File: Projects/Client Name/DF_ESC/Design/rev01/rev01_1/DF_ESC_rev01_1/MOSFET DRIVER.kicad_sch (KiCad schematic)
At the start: 40 parts, among them U1 DRV8302DCAR

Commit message: Update 2024-02-28_2
Input Proteccion Done
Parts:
- renumbered C2 to C?, C4 to C?, C3 to C?, D1 to D?, U1 to U?

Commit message: Update 2024-02-03
Schematic finish but DRC CHEK Errors
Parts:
- removed U?: DRV8302DCAR, DCA56_6P35X3P61, symbol DRV8302:DRV8302DCAR
- added U3: DRV8302DCAR, footprint:HTSSOP-56_L14.0-W6.1-P0.50-LS8.1-BL-EP, symbol Motor_Driver:DRV8302DCAR
- C26, C27, C28, C29, C30, C31, C32, C33, C34, C35, C36, C37, C38, C39, C40, C41, C42, C43, C44, C45, C46, C47, C48, C49: renamed from C?; footprint (none) -> Capacitor_SMD:C_0603_1608Metric_Pad1.08x0.95mm_HandSolder
- L1: renamed from L?; footprint (none) -> DF_ESC_Footprint_Library_Casa:IND-SMD_L7.8-W7.8_SDR0805
- R17, R18, R19, R20, R21, R22, R23, R24, R25, R26, R27, R28: renamed from R?; footprint (none) -> Resistor_SMD:R_0603_1608Metric_Pad0.98x0.95mm_HandSolder
- gave numbers to parts that had none: 2
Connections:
- net +3V3: now also U3.24 (REF), U3.9 (M_OC)
- net +VDC: now also U3.29 (PVDD1), U3.53 (PVDD2), U3.54 (PVDD2)
- net BIAS: now also U3.49 (BIAS)
- net BR_S01: now also U3.25 (SO1)
- net BR_S02: now also U3.26 (SO2)
- net BST_A: now also U3.48 (BST_A)
- net BST_B: now also U3.43 (BST_B)
- net BST_BK: now also U3.52 (BST_BK)
- net BST_C: now also U3.38 (BST_C)
- net COMP: now also U3.2 (COMP)
- net CP1: now also U3.14 (CP1)
- net CP2: now also U3.15 (CP2)
- net DC_CAL: now also U3.12 (DC_CAL)
- net DTC: now also U3.7 (DTC)
- net DVDD: now also U3.11 (OC_ADJ), U3.23 (DVDD)
- net EN_GATE: now also U3.16 (EN_GATE)
- net FAULT: now also U3.6 (nFAULT)
- net GND: now also U3.10 (GAIN), U3.28 (AGND), U3.57 (GND), U3.8 (M_PWM)
- net GVDD: now also U3.13 (GVDD)
- net H1: now also U3.17 (INH_A)
- net H1_LOW: now also U3.44 (SL_A)
- net H1_VS: now also U3.46 (SH_A)
- net H2: now also U3.19 (INH_B)
- net H2_LOW: now also U3.39 (SL_B)
- net H2_VS: now also U3.41 (SH_B)
- net H3: now also U3.21 (INH_C)
- net H3_LOW: now also U3.34 (SL_C)
- net H3_VS: now also U3.36 (SH_C)
- net L1: now also U3.18 (INL_A)
- net L2: now also U3.20 (INL_B)
- net L3: now also U3.22 (INL_C)
- net M_H1: now also U3.47 (GH_A)
- net M_H2: now also U3.42 (GH_B)
- net M_H3: now also U3.37 (GH_C)
- net M_L1: now also U3.45 (GL_A)
- net M_L2: now also U3.40 (GL_B)
- net M_L3: now also U3.35 (GL_C)
- net PH: now also U3.50 (PH), U3.51 (PH)
- net RT_CLK: now also U3.1 (RT_CLK)
- net S1_N: now also U3.33 (SN1)
- net S1_P: now also U3.32 (SP1)
- net S2_N: now also U3.31 (SN2)
- net S2_P: now also U3.30 (SP2)
- net VSENSE: now also U3.3 (VSENSE)
- net at C33.1: now also U3.27 (AVDD)
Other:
- moved on the sheet: C36, D10, L1, R20

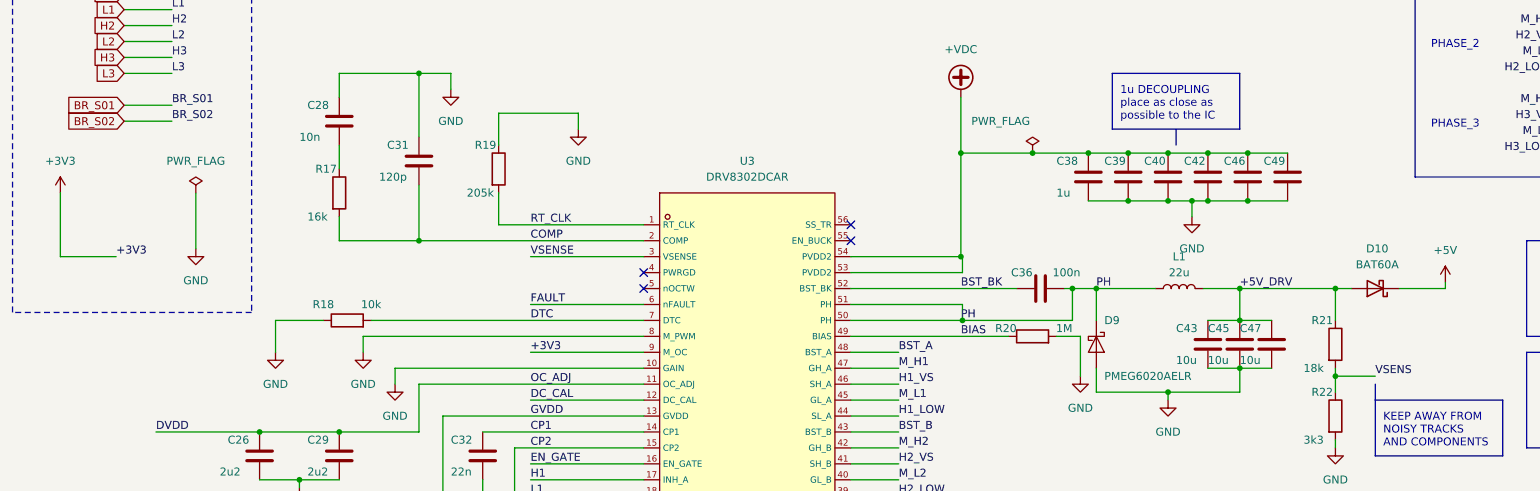
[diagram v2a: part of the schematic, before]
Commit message: Update 2024-03-03
ERC 0 Errors. Update PCB from schematics prepare to going on
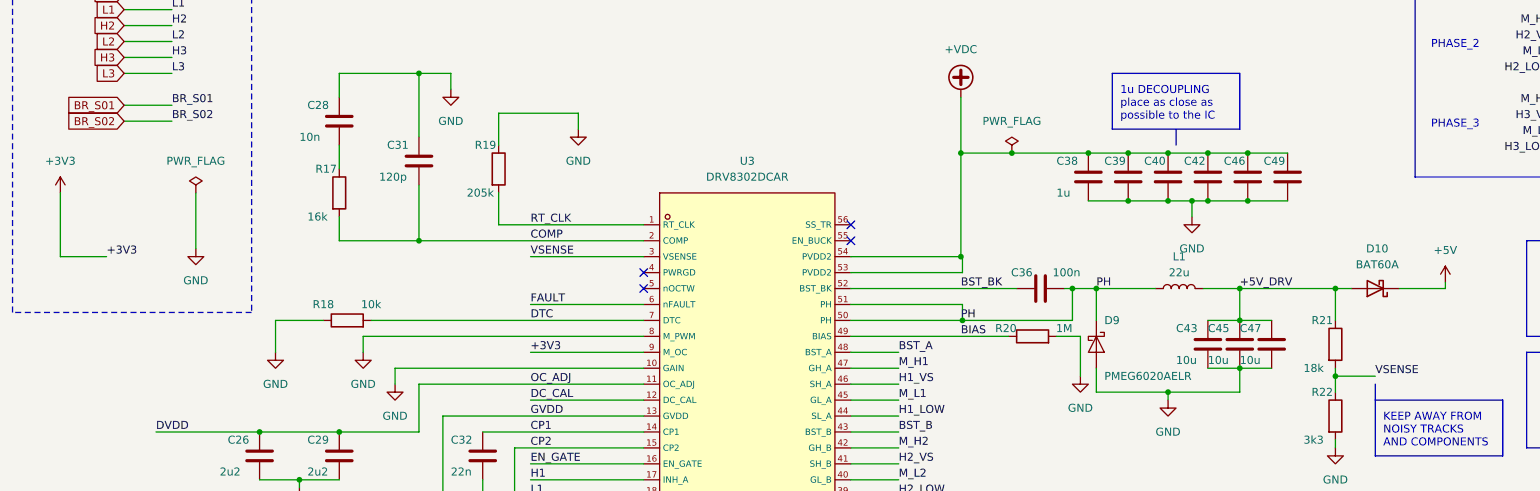
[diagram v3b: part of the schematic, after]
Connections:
- net VSENS is gone; now on net VSENSE: R21.2, R22.1
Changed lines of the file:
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@@
   (junction (at 165.1 144.78) (diameter 0) (color 0 0 0 0)
   )
-  (junction (at 176.53 64.77) (diameter 0) (color 0 0 0 0)
-  )
   (junction (at 191.77 72.39) (diameter 0) (color 0 0 0 0)
   )
@@
   )
   (junction (at 165.354 91.44) (diameter 0) (color 0 0 0 0)
+  )
+  (junction (at 173.228 64.77) (diameter 0) (color 0 0 0 0)
   )
   (junction (at 177.8 144.78) (diameter 0) (color 0 0 0 0)
@@
     (stroke (width 0) (type default))
   )
-  (wire (pts (xy 165.1 64.77) (xy 176.53 64.77))
+  (wire (pts (xy 165.1 64.77) (xy 173.228 64.77))
     (stroke (width 0) (type default))
   )
@@
     (stroke (width 0) (type default))
   )
-  (wire (pts (xy 21.59 81.28) (xy 30.48 81.28))
+  (wire (pts (xy 21.59 81.28) (xy 28.956 81.28))
     (stroke (width 0) (type default))
   )
@@
     (stroke (width 0) (type default))
   )
+  (wire (pts (xy 173.228 64.77) (xy 185.42 64.77))
+    (stroke (width 0) (type default))
+  )
   (wire (pts (xy 66.04 55.88) (xy 66.04 52.07))
     (stroke (width 0) (type default))
@@
   )
   (wire (pts (xy 96.52 139.7) (xy 114.554 139.7))
-    (stroke (width 0) (type default))
-  )
-  (wire (pts (xy 176.53 64.77) (xy 185.42 64.77))
     (stroke (width 0) (type default))
   )
@@
     (effects (font (size 1.27 1.27)) (justify right bottom))
   )
-  (label "+3V3" (at 30.48 81.28 0) (fields_autoplaced)
+  (label "+3V3" (at 28.956 81.28 0) (fields_autoplaced)
     (effects (font (size 1.27 1.27)) (justify left bottom))
   )
@@
     (effects (font (size 1.27 1.27)) (justify left bottom))
   )
-  (label "VSENS" (at 231.14 100.33 0) (fields_autoplaced)
+  (label "VSENSE" (at 231.14 100.33 0) (fields_autoplaced)
     (effects (font (size 1.27 1.27)) (justify left bottom))
   )
@@
     )
   )
+  (symbol (lib_id "power:PWR_FLAG") (at 43.18 71.12 0) (unit 1)
+    (in_bom yes) (on_board yes) (dnp no) (fields_autoplaced)
+    (property "Reference" "#FLG01" (at 43.18 69.215 0)
+      (effects (font (size 1.27 1.27)) hide)
+    )
+    (property "Value" "PWR_FLAG" (at 43.18 66.04 0)
+      (effects (font (size 1.27 1.27)))
+    )
+    (property "Footprint" "" (at 43.18 71.12 0)
+      (effects (font (size 1.27 1.27)) hide)
+    )
+    (property "Datasheet" "~" (at 43.18 71.12 0)
+      (effects (font (size 1.27 1.27)) hide)
+    )
+    (pin "1")
+    (instances
+      (project "DF_ESC_rev01_1"
+        (path "/e63e39d7-6ac0-4ffd-8aa3-1841a4541b55/ebfeafe7-4d70-4ef9-bb18-a00f088a6e19"
+          (reference "#FLG01") (unit 1)
+        )
+      )
+    )
+  )
   (symbol (lib_id "power:GND") (at 83.82 54.61 0) (unit 1)
     (in_bom yes) (on_board yes) (dnp no) (fields_autoplaced)
@@
     )
   )
+  (symbol (lib_id "power:PWR_FLAG") (at 173.228 64.77 0) (unit 1)
+    (in_bom yes) (on_board yes) (dnp no) (fields_autoplaced)
+    (property "Reference" "#FLG02" (at 173.228 62.865 0)
+      (effects (font (size 1.27 1.27)) hide)
+    )
+    (property "Value" "PWR_FLAG" (at 173.228 59.69 0)
+      (effects (font (size 1.27 1.27)))
+    )
+    (property "Footprint" "" (at 173.228 64.77 0)
+      (effects (font (size 1.27 1.27)) hide)
+    )
+    (property "Datasheet" "~" (at 173.228 64.77 0)
+      (effects (font (size 1.27 1.27)) hide)
+    )
+    (pin "1")
+    (instances
+      (project "DF_ESC_rev01_1"
+        (path "/e63e39d7-6ac0-4ffd-8aa3-1841a4541b55/ebfeafe7-4d70-4ef9-bb18-a00f088a6e19"
+          (reference "#FLG02") (unit 1)
+        )
+      )
+    )
+  )
   (symbol (lib_id "Device:R") (at 91.44 67.31 0) (unit 1)
     (in_bom yes) (on_board yes) (dnp no)
@@
         (path "/e63e39d7-6ac0-4ffd-8aa3-1841a4541b55/ebfeafe7-4d70-4ef9-bb18-a00f088a6e19"
           (reference "#PWR044") (unit 1)
-        )
-      )
-    )
-  )
-  (symbol (lib_id "power:PWR_FLAG") (at 176.53 64.77 0) (unit 1)
-    (in_bom yes) (on_board yes) (dnp no)
-    (property "Reference" "#FLG02" (at 176.53 62.865 0)
-      (effects (font (size 1.27 1.27)) hide)
-    )
-    (property "Value" "PWR_FLAG" (at 171.45 59.69 0)
-      (effects (font (size 1.27 1.27)))
-    )
-    (property "Footprint" "" (at 176.53 64.77 0)
-      (effects (font (size 1.27 1.27)) hide)
-    )
-    (property "Datasheet" "~" (at 176.53 64.77 0)
-      (effects (font (size 1.27 1.27)) hide)
-    )
-    (pin "1")
-    (instances
-      (project "DF_ESC_rev01_1"
-        (path "/e63e39d7-6ac0-4ffd-8aa3-1841a4541b55/ebfeafe7-4d70-4ef9-bb18-a00f088a6e19"
-          (reference "#FLG02") (unit 1)
         )
       )
@@
         )
       )
-    )
-  )
-  (symbol (lib_id "power:PWR_FLAG") (at 43.18 71.12 0) (unit 1)
-    (in_bom yes) (on_board yes) (dnp no) (fields_autoplaced)
-    (property "Reference" "#FLG01" (at 43.18 69.215 0)
-      (effects (font (size 1.27 1.27)) hide)
-    )
-    (property "Value" "PWR_FLAG" (at 43.18 66.04 0)
-      (effects (font (size 1.27 1.27)))
-    )
-    (property "Footprint" "" (at 43.18 71.12 0)
-      (effects (font (size 1.27 1.27)) hide)
-    )
-    (property "Datasheet" "~" (at 43.18 71.12 0)
-      (effects (font (size 1.27 1.27)) hide)
-    )
-    (pin "1")
-    (instances
-      (project "DF_ESC_rev01_1"
-        (path "/e63e39d7-6ac0-4ffd-8aa3-1841a4541b55/ebfeafe7-4d70-4ef9-bb18-a00f088a6e19"
-          (reference "#FLG01") (unit 1)
-        )
-      )
